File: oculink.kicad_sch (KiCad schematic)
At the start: 3 parts, among them J1 OCuLink_x4_Amphenol_G14A42121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

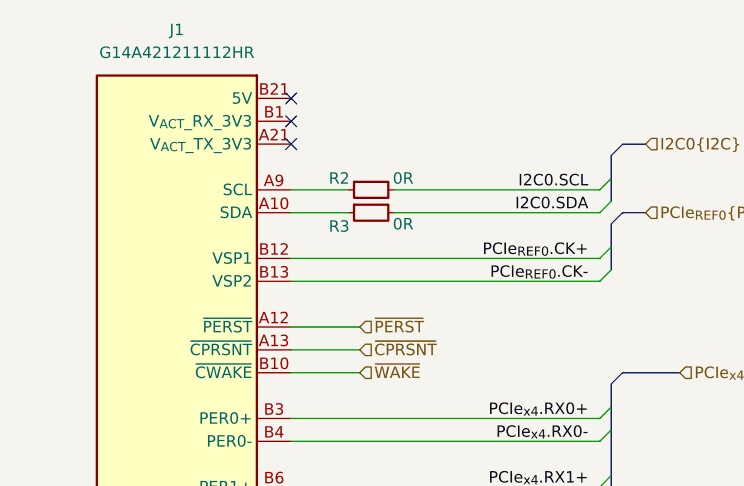
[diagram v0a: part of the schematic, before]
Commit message: [#79026] Add power supply section, reannotate schematic
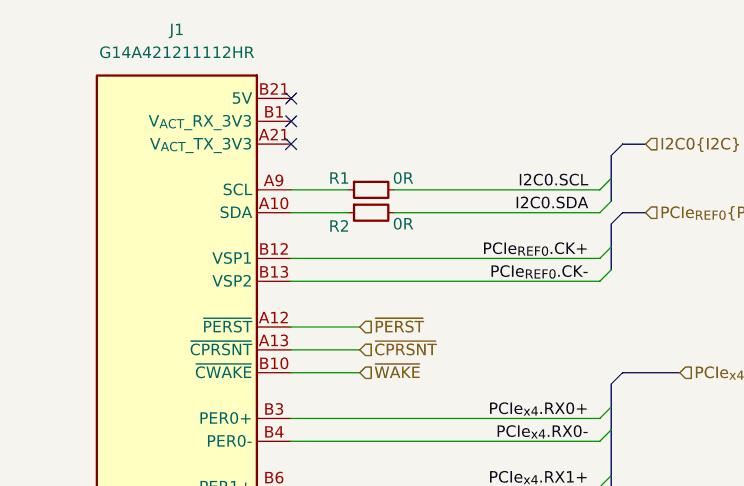
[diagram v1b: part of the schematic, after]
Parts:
- renumbered R2 to R1, R3 to R2
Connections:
- net at J1.A9 (NC): now also R1.1
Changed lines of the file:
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@@
 		(on_board yes)
 		(dnp no)
-		(property "Reference" "R3"
+		(property "Reference" "R2"
 			(at 202.184 106.934 0)
 			(effects
@@
 			(project "oculink-to-pcie-adapter"
 				(path "/44c3be85-0a18-4d93-a9a5-650ee09b6032/642de475-f425-453b-bd11-9d34133bc8d0"
-					(reference "R3")
+					(reference "R2")
 					(unit 1)
 				)
@@
 		(on_board yes)
 		(dnp no)
-		(property "Reference" "#PWR075"
+		(property "Reference" "#PWR02"
 			(at 160.02 189.23 0)
 			(effects
@@
 			(project "oculink-to-pcie-adapter"
 				(path "/44c3be85-0a18-4d93-a9a5-650ee09b6032/642de475-f425-453b-bd11-9d34133bc8d0"
-					(reference "#PWR075")
+					(reference "#PWR02")
 					(unit 1)
 				)
@@
 		(on_board yes)
 		(dnp no)
-		(property "Reference" "R2"
+		(property "Reference" "R1"
 			(at 202.184 101.6 0)
 			(effects
@@
 			(project "oculink-to-pcie-adapter"
 				(path "/44c3be85-0a18-4d93-a9a5-650ee09b6032/642de475-f425-453b-bd11-9d34133bc8d0"
-					(reference "R2")
+					(reference "R1")
 					(unit 1)
 				)

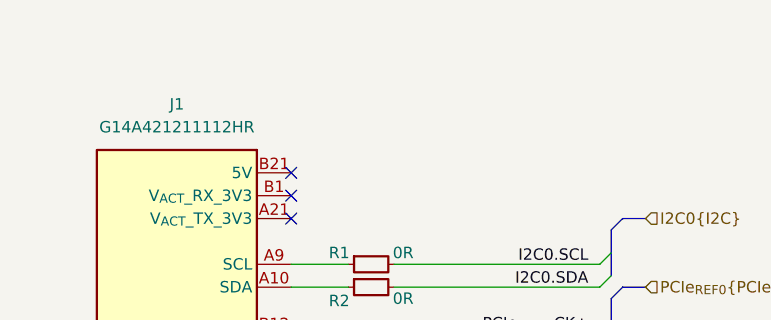
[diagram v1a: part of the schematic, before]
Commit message: [#79026] Change power input connector, add net classes, minor schematic refactor
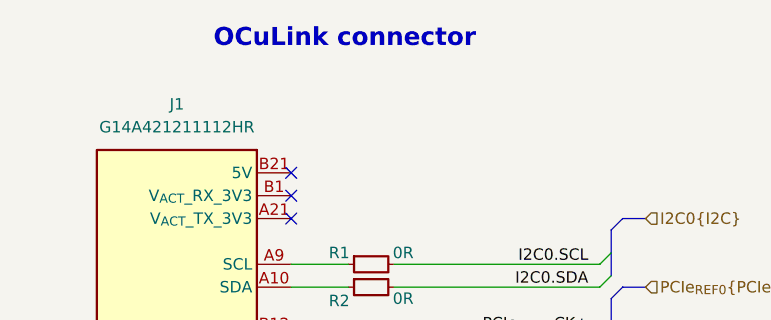
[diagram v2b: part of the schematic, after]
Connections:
- net at J1.A9 (SCL): now also R1.1
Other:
- note added: "OCuLink connector"
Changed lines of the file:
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@@
 		(members "CK+" "CK-")
+	)
+	(text "OCuLink connector"
+		(exclude_from_sim no)
+		(at 188.214 78.994 0)
+		(effects
+			(font
+				(size 2 2)
+				(thickness 0.4)
+				(bold yes)
+			)
+			(justify left bottom)
+		)
 	)
 	(junction
@@
 			)
 			(justify left)
+		)
+	)
+	(rule_area
+		(polyline
+			(pts
+				(xy 215.9 106.68) (xy 257.81 106.68) (xy 257.81 115.57) (xy 215.9 115.57)
+			)
+			(stroke
+				(width 0)
+				(type dash)
+			)
+			(fill
+				(type none)
+			)
+		)
+	)
+	(rule_area
+		(polyline
+			(pts
+				(xy 215.9 120.65) (xy 257.81 120.65) (xy 257.81 186.69) (xy 215.9 186.69)
+			)
+			(stroke
+				(width 0)
+				(type dash)
+			)
+			(fill
+				(type none)
+			)
+		)
+	)
+	(netclass_flag ""
+		(length 2.54)
+		(shape round)
+		(at 257.81 106.68 0)
+		(fields_autoplaced yes)
+		(effects
+			(font
+				(size 1.27 1.27)
+				(color 0 132 132 1)
+			)
+			(justify left bottom)
+		)
+		(property "Netclass" "PCIe_{REF}"
+			(at 258.5085 104.14 0)
+			(effects
+				(font
+					(size 1.27 1.27)
+				)
+				(justify left)
+			)
+		)
+		(property "Component Class" ""
+			(at -114.3 -8.89 0)
+			(effects
+				(font
+					(size 1.27 1.27)
+					(italic yes)
+				)
+			)
+		)
+	)
+	(netclass_flag ""
+		(length 2.54)
+		(shape round)
+		(at 257.81 120.65 0)
+		(fields_autoplaced yes)
+		(effects
+			(font
+				(size 1.27 1.27)
+				(color 0 132 0 1)
+			)
+			(justify left bottom)
+		)
+		(property "Netclass" "PCIe"
+			(at 258.5085 118.11 0)
+			(effects
+				(font
+					(size 1.27 1.27)
+				)
+				(justify left)
+			)
+		)
+		(property "Component Class" ""
+			(at -114.3 5.08 0)
+			(effects
+				(font
+					(size 1.27 1.27)
+					(italic yes)
+				)
+			)
 		)
 	)
@@
 		(pin "A15"
 		)
-		(pin "A9"
+		(pin "B9"
 		)
 		(pin "B2"

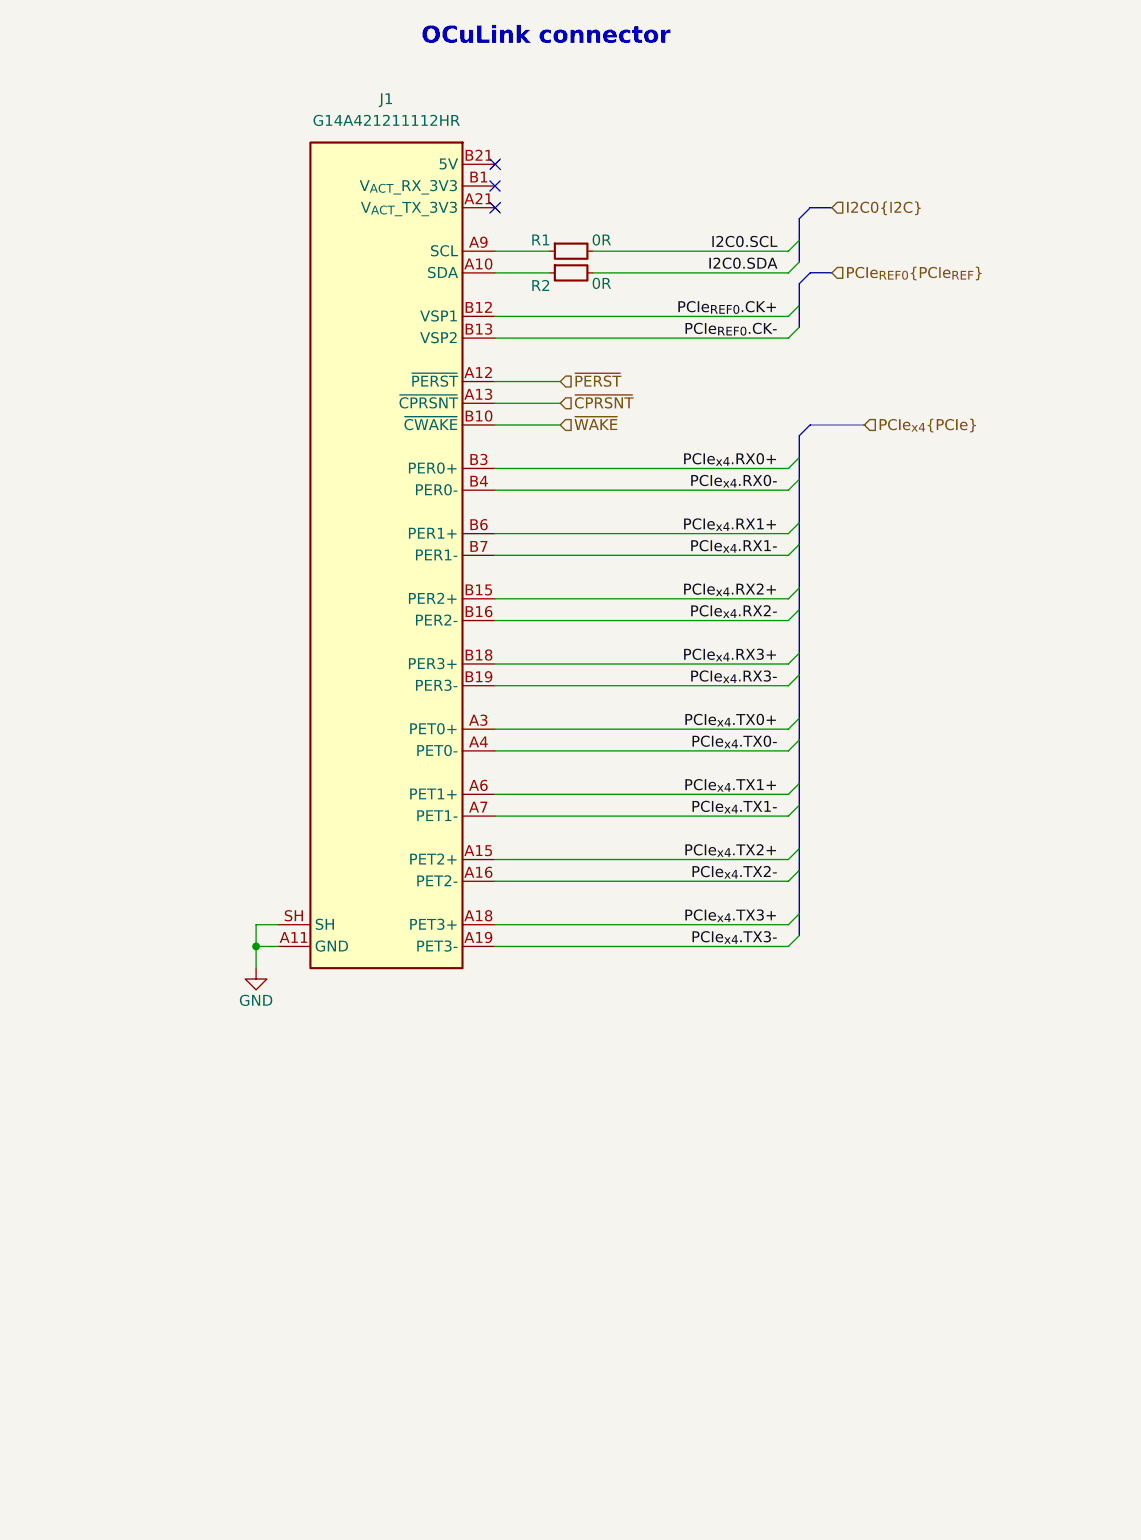
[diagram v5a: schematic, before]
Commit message: [#79262] Add TVS to OCuLink connector, add decoupling capacitors for PCIe connector
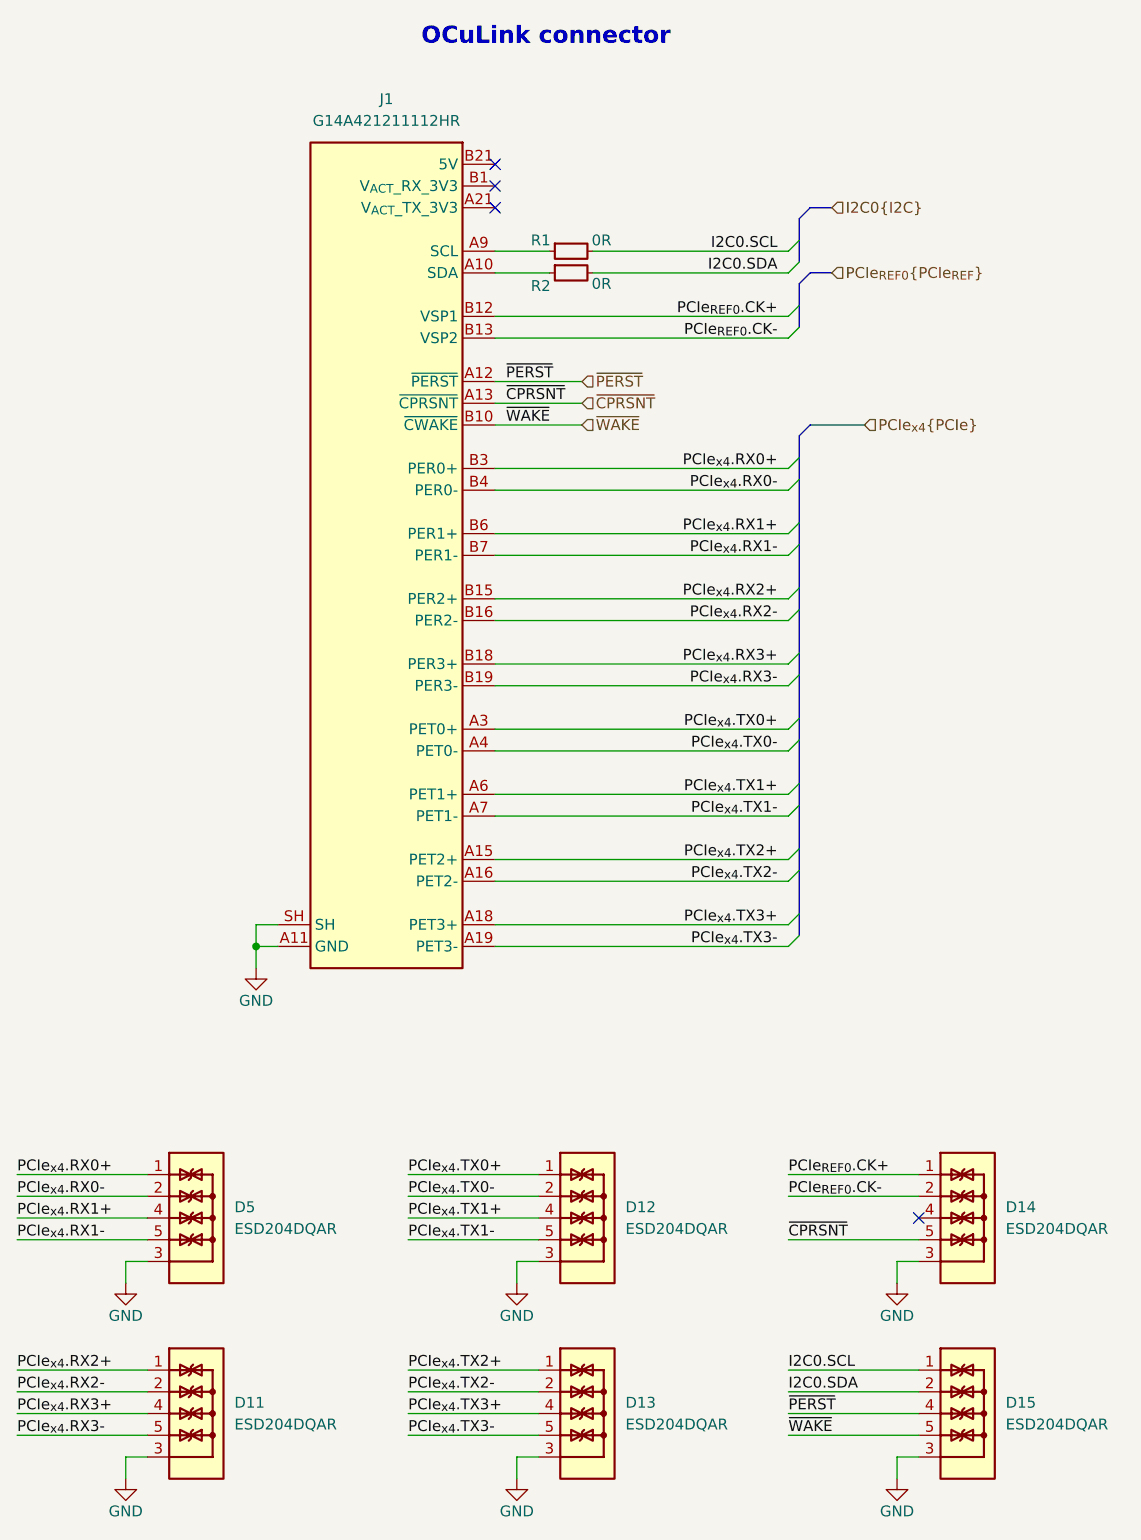
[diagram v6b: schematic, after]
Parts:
- added D11, D12, D13, D14, D15, D5: ESD204DQAR, antmicro-footprints:USON-10_2.5x1mm_P0.5mm, symbol antmicroTVSDiodes:ESD204DQAR
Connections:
- net GND: now also D11.3, D11.8, D12.3, D12.8, D13.3, D13.8, D14.3, D14.8, D15.3, D15.8, D5.3, D5.8
- net I2C0.SCL: now also D15.1, D15.10
- net I2C0.SDA: now also D15.2, D15.9
- net PCIe_{REF0}.CK+: now also D14.1, D14.10
- net PCIe_{REF0}.CK-: now also D14.2, D14.9
- net PCIe_{x4}.RX0+: now also D5.1, D5.10
- net PCIe_{x4}.RX0-: now also D5.2, D5.9
- net PCIe_{x4}.RX1+: now also D5.4, D5.7
- net PCIe_{x4}.RX1-: now also D5.5, D5.6
- net PCIe_{x4}.RX2+: now also D11.1, D11.10
- net PCIe_{x4}.RX2-: now also D11.2, D11.9
- net PCIe_{x4}.RX3+: now also D11.4, D11.7
- net PCIe_{x4}.RX3-: now also D11.5, D11.6
- net PCIe_{x4}.TX0+: now also D12.1, D12.10
- net PCIe_{x4}.TX0-: now also D12.2, D12.9
- net PCIe_{x4}.TX1+: now also D12.4, D12.7
- net PCIe_{x4}.TX1-: now also D12.5, D12.6
- net PCIe_{x4}.TX2+: now also D13.1, D13.10
- net PCIe_{x4}.TX2-: now also D13.2, D13.9
- net PCIe_{x4}.TX3+: now also D13.4, D13.7
- net PCIe_{x4}.TX3-: now also D13.5, D13.6
- net ~{CPRSNT}: now also D14.5, D14.6
- net ~{PERST}: now also D15.4, D15.7
- net ~{WAKE}: now also D15.5, D15.6
- new net: D14.4, D14.7
- no-connect marks 3 -> 4
